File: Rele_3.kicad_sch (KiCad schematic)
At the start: 6 parts, among them J17 Rele_3, J35 Pin GND, K6 SRD-05VDC-SL-C, Q14 PMBT3904,235

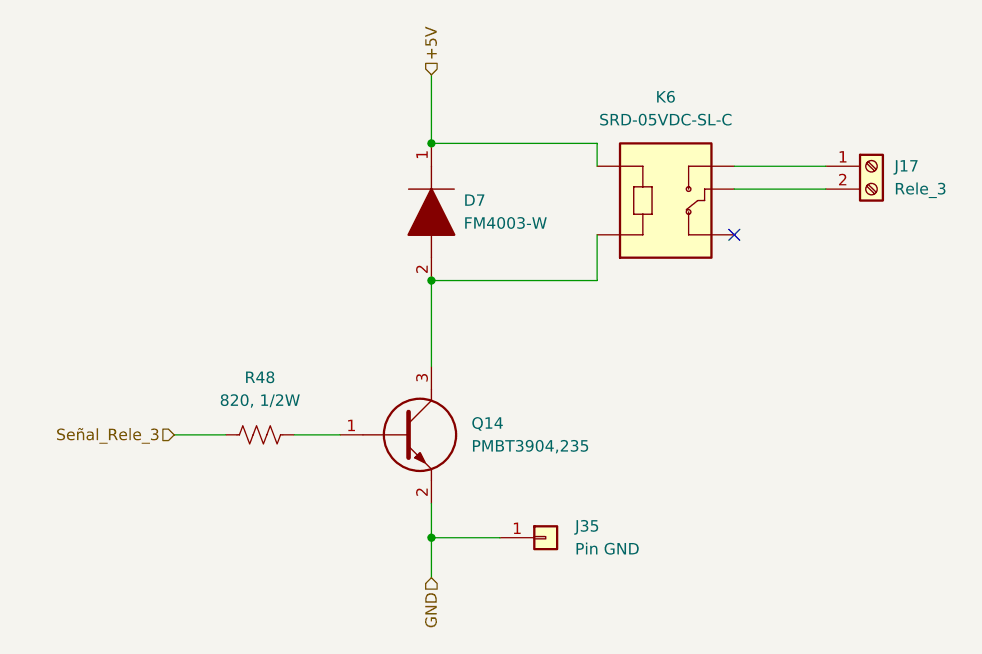
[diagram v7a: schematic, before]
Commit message: Se modificaron algunos componentes, según disponibilidad
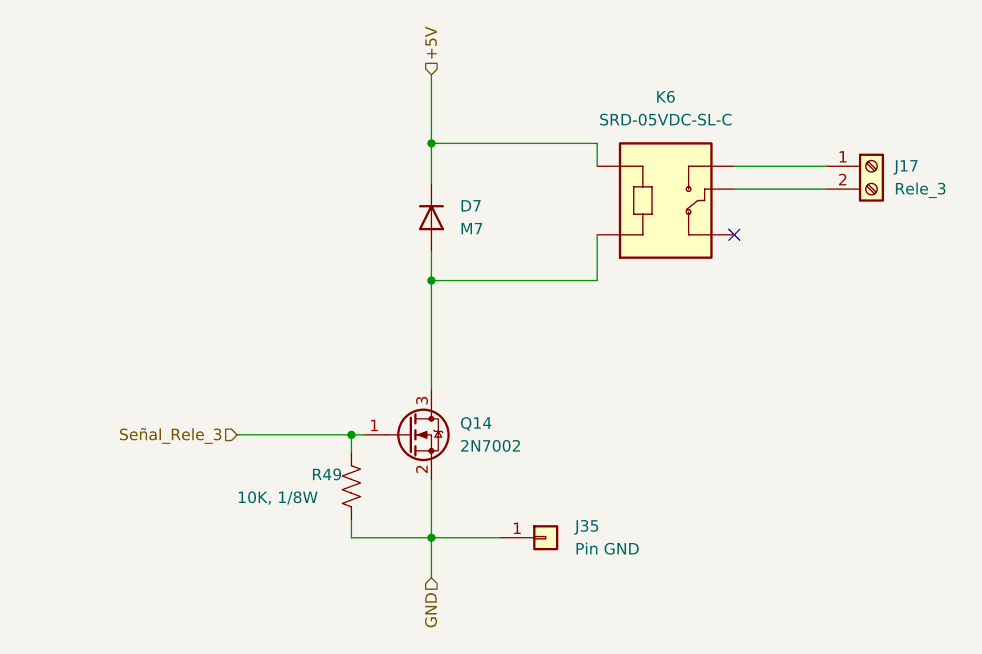
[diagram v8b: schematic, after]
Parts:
- removed D7: FM4003-W, FM4003W:DIOM5025X231N, symbol FM4003-W:FM4003-W
- removed Q14: PMBT3904,235, PMBT3904,235:SOT95P230X110-3N, symbol PMBT3904,235:PMBT3904,235
- removed R48: 820, 1/2W, Resistor_SMD:R_0805_2012Metric, symbol Device:R_US
- added D7: M7, Diode_SMD:D_SMA, symbol Device:D
- added Q14: 2N7002, Package_TO_SOT_SMD:SOT-23, symbol Transistor_FET:2N7002
- added R49: 10K, 1/8W, Resistor_SMD:R_0805_2012Metric, symbol Device:R_US
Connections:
- net +5V: now also D7.1 (K)
- net GND: now also Q14.2 (S), R49.2
- net Señal_Rele_3: now also Q14.1 (G), R49.1
- net at K6.A2: now also D7.2 (A), Q14.3 (D)
